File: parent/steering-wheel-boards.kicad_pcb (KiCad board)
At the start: 4 copper layers, 109.5 x 52 mm, 84 parts, among them J1 Conn_01x08, J2 Conn_01x06, J3 Conn_01x06, J4 Conn_01x04, Q1 2N2222A, Q2 2N2222A, U1 LM317_TO-220, U3 TLC5951DAP, U4 MCP2551-I-SN

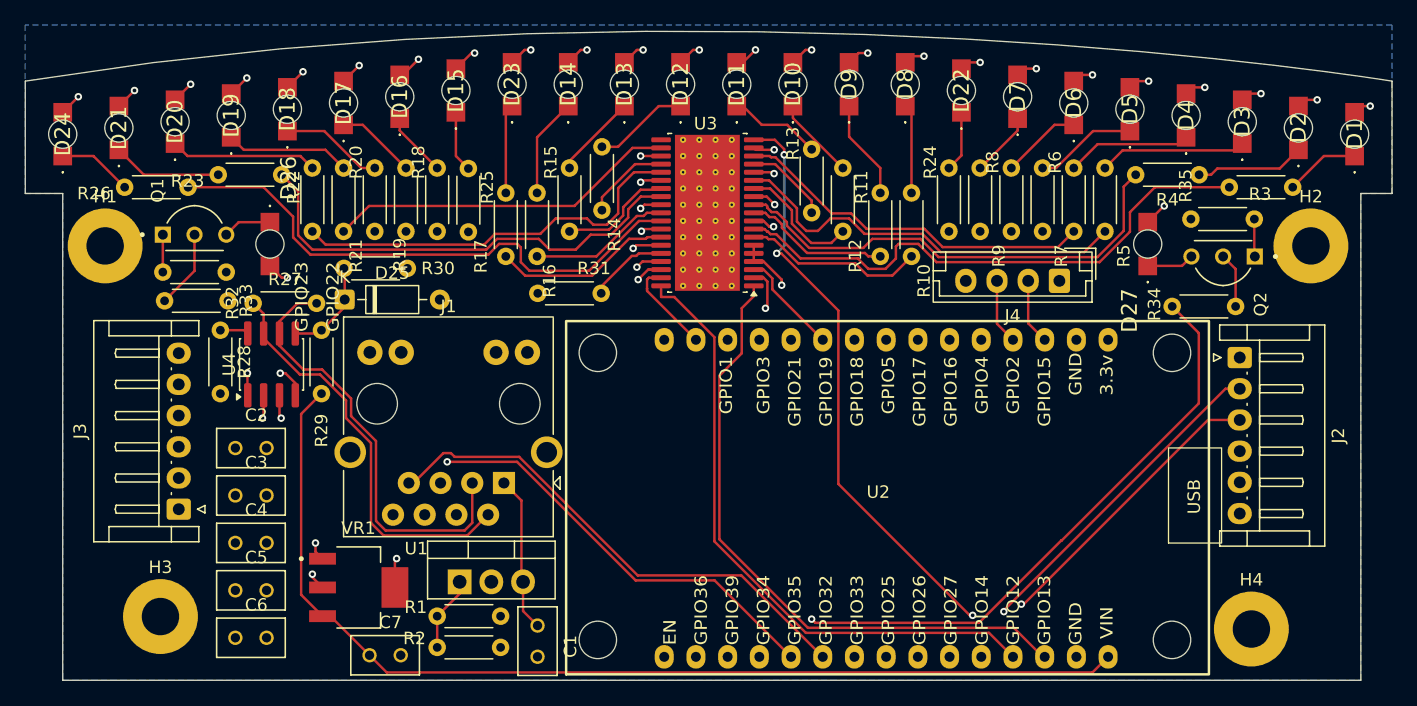
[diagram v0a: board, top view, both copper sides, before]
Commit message: Route Steering Wheel
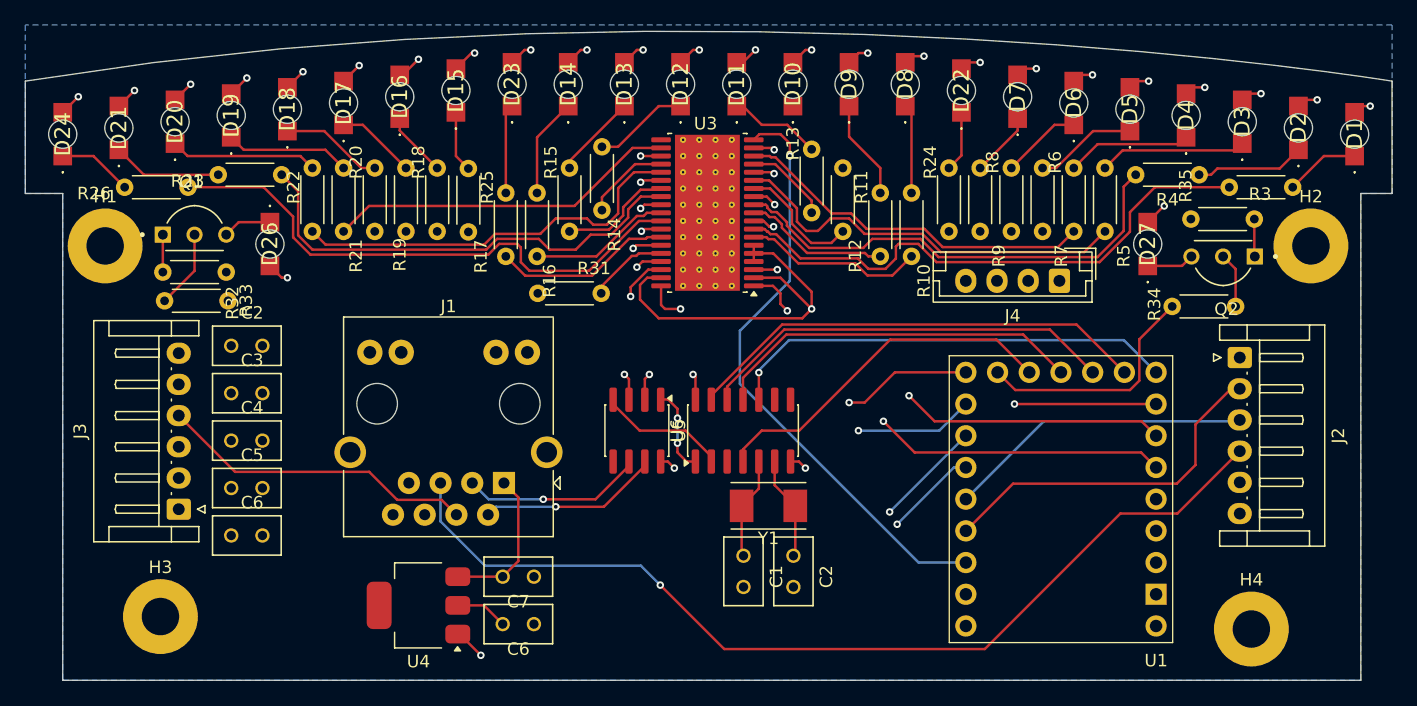
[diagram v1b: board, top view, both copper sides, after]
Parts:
- removed D25: 2.4, Diode_THT:D_DO-35_SOD27_P7.62mm_Horizontal
- removed R1: 240, Resistor_THT:R_Axial_DIN0204_L3.6mm_D1.6mm_P5.08mm_Horizontal
- removed R2: 5k, Resistor_THT:R_Axial_DIN0204_L3.6mm_D1.6mm_P5.08mm_Horizontal
- removed R27: 120, Resistor_THT:R_Axial_DIN0204_L3.6mm_D1.6mm_P5.08mm_Horizontal
- removed R28: R, Resistor_THT:R_Axial_DIN0204_L3.6mm_D1.6mm_P5.08mm_Horizontal
- removed R29: 1k, Resistor_THT:R_Axial_DIN0204_L3.6mm_D1.6mm_P5.08mm_Horizontal
- removed R30: R_Variable, Resistor_THT:R_Axial_DIN0204_L3.6mm_D1.6mm_P5.08mm_Horizontal
- removed U2: ~, FBR_Footprints:ESP32_30pin
- removed VR1: LM3940IMP-3.3_NOPB, FBR_Footprints:SOT230P700X180-4N
- added C2: 32p, SteeringWheel:CAP_RCER72A105K2DBH03A, F.Cu at (165.5, 67.3)
- added C6: 100u, SteeringWheel:CAP_RCER72A105K2DBH03A, F.Cu at (143.5, 71.5)
- added U5: MCP2561-E-SN, Package_SO:SOIC-8_3.9x4.9mm_P1.27mm, F.Cu at (153.0, 56.0)
- added U6: MCP2517FD-xSL, Package_SO:SOIC-14_3.9x8.7mm_P1.27mm, F.Cu at (161.5, 56.0)
- added Y1: ABM7-20.000MHZ-D2Y-T, Crystal:Crystal_SMD_Abracon_ABM7-2Pin_6.0x3.5mm, F.Cu at (163.5, 62.0)
- C1: value 0.1u -> 32p; footprint FBR_Footprints:CAP_RCER72A105K2DBH03A -> SteeringWheel:CAP_RCER72A105K2DBH03A
- C3, C4, C5: footprint FBR_Footprints:CAP_RCER72A105K2DBH03A -> SteeringWheel:CAP_RCER72A105K2DBH03A
- C7: value 33u -> 10u; footprint FBR_Footprints:CAP_RCER72A105K2DBH03A -> SteeringWheel:CAP_RCER72A105K2DBH03A
- D1, D10, D11, D12, D13, D14, D15, D16, D17, D18, D19, D2, D20, D21, D22, D23, D24, D26, D27, D3, D4, D5, D6, D7, D8, D9: footprint FBR_Footprints:5990K80107F -> SteeringWheel:5990K80107F
- Q1, Q2: footprint FBR_Footprints:2N2222A -> SteeringWheel:2N2222A
- U1: value LM317_TO-220 -> ~; footprint Package_TO_SOT_THT:TO-220-3_Vertical -> SteeringWheel:RP2350_Zero
- U4: value MCP2551-I-SN -> LT1117-5.0; footprint Package_SO:SOIC-8_3.9x4.9mm_P1.27mm -> Package_TO_SOT_SMD:SOT-223
- moved U1 55.9 mm to (194.6, 71.7), turned to 180 degrees
- moved U4 22.6 mm to (135.5, 70.0), turned to 180 degrees
- moved C1 17.4 mm to (161.5, 67.3)
- moved C7 12.4 mm to (143.5, 67.7)
- moved C4 8.20 mm to (121.8, 56.8)
- moved C2 8.20 mm to (121.8, 49.2)
- moved C3 8.20 mm to (121.8, 53.0)
- moved C5 8.20 mm to (121.8, 60.6)
- moved C6 8.20 mm to (121.8, 64.4)
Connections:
- C1 pad 1: +12V -> Net-(U6-OSC2)
- C7 pad 1: +3V3 -> VCONN
- J1 pad 1: +12V -> VCONN
- U1 pad 1: Net-(U1-ADJ) -> /GSSIN
- U1 pad 2: +5V -> /DCSIN
- U1 pad 3: +12V -> /GSSOUT
- U4 pad 1: /CAN_TX -> GND
- U4 pad 2: GND -> +5V
- U4 pad 3: +5V -> VCONN
- U4 pad 4: /CAN_RX -> (no net)
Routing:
- net +3V3: track 84.5 -> 0.00 mm
- net /CS: track 0.00 -> 37.4 mm
- net /UC_CLK: track 27.4 -> 63.9 mm
- net /SCK: track 0.00 -> 36.3 mm, vias 0 -> 1
- net /CAN_TX: track 42.2 -> 6.91 mm, vias 1 -> 2
- net /MISO: track 0.00 -> 33.6 mm
- net /LED_E2: track 52.5 -> 19.3 mm, vias 1 -> 0
- net /CAN_RX: track 42.8 -> 10.4 mm, vias 1 -> 0
- net /MOSI: track 0.00 -> 29.9 mm
- net /XBLNK: track 21.7 -> 51.5 mm, vias 1 -> 2
- net /GSLAT: track 8.37 -> 37.7 mm, vias 0 -> 2
- net /INT: track 0.00 -> 28.6 mm
- net /CAN_LOW: track 35.1 -> 14.6 mm, vias 0 -> 1
- net /I2C_SCL: track 5.25 -> 25.3 mm
- net /CAN_HIGH: track 33.4 -> 14.5 mm, vias 0 -> 1
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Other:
- board text removed: "GND"
- board text removed: "GPIO12"
- board text removed: "GPIO13"
- board text removed: "GPIO14"
- board text removed: "GPIO25"
- board text removed: "GPIO26"
- board text removed: "GPIO27"
- board text removed: "GPIO33"

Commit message: Change input voltage to +5V
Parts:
- removed the C2 at (121.8, 49.2)
- removed C6: 0.47u, FBR_Footprints:CAP_RCER72A105K2DBH03A
- removed C6: 100u, SteeringWheel:CAP_RCER72A105K2DBH03A
- removed C7: 10u, SteeringWheel:CAP_RCER72A105K2DBH03A
- removed U4: LT1117-5.0, Package_TO_SOT_SMD:SOT-223
- U1: value ~ -> RP2350_Zero
- moved C3 31.3 mm to (152.8, 49.0), turned to 180 degrees
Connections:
- J1 pad 1: VCONN -> +5V
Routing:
- net VCONN: track 12.1 -> 0.00 mm
- net Net-(D10-K): track 0.00 -> 6.62 mm
- net GND: track 9.79 -> 7.24 mm, vias 5 -> 4
- net +5V: track 57.3 -> 55.8 mm, vias 29 -> 28
